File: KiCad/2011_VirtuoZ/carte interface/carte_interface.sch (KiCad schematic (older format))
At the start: 56 parts, among them P10 Convertisseur_I, P11 Convertisseur_U, P12 Convertisseur_PWM, P9 Vitesse, U3 LM358, U4 LM358

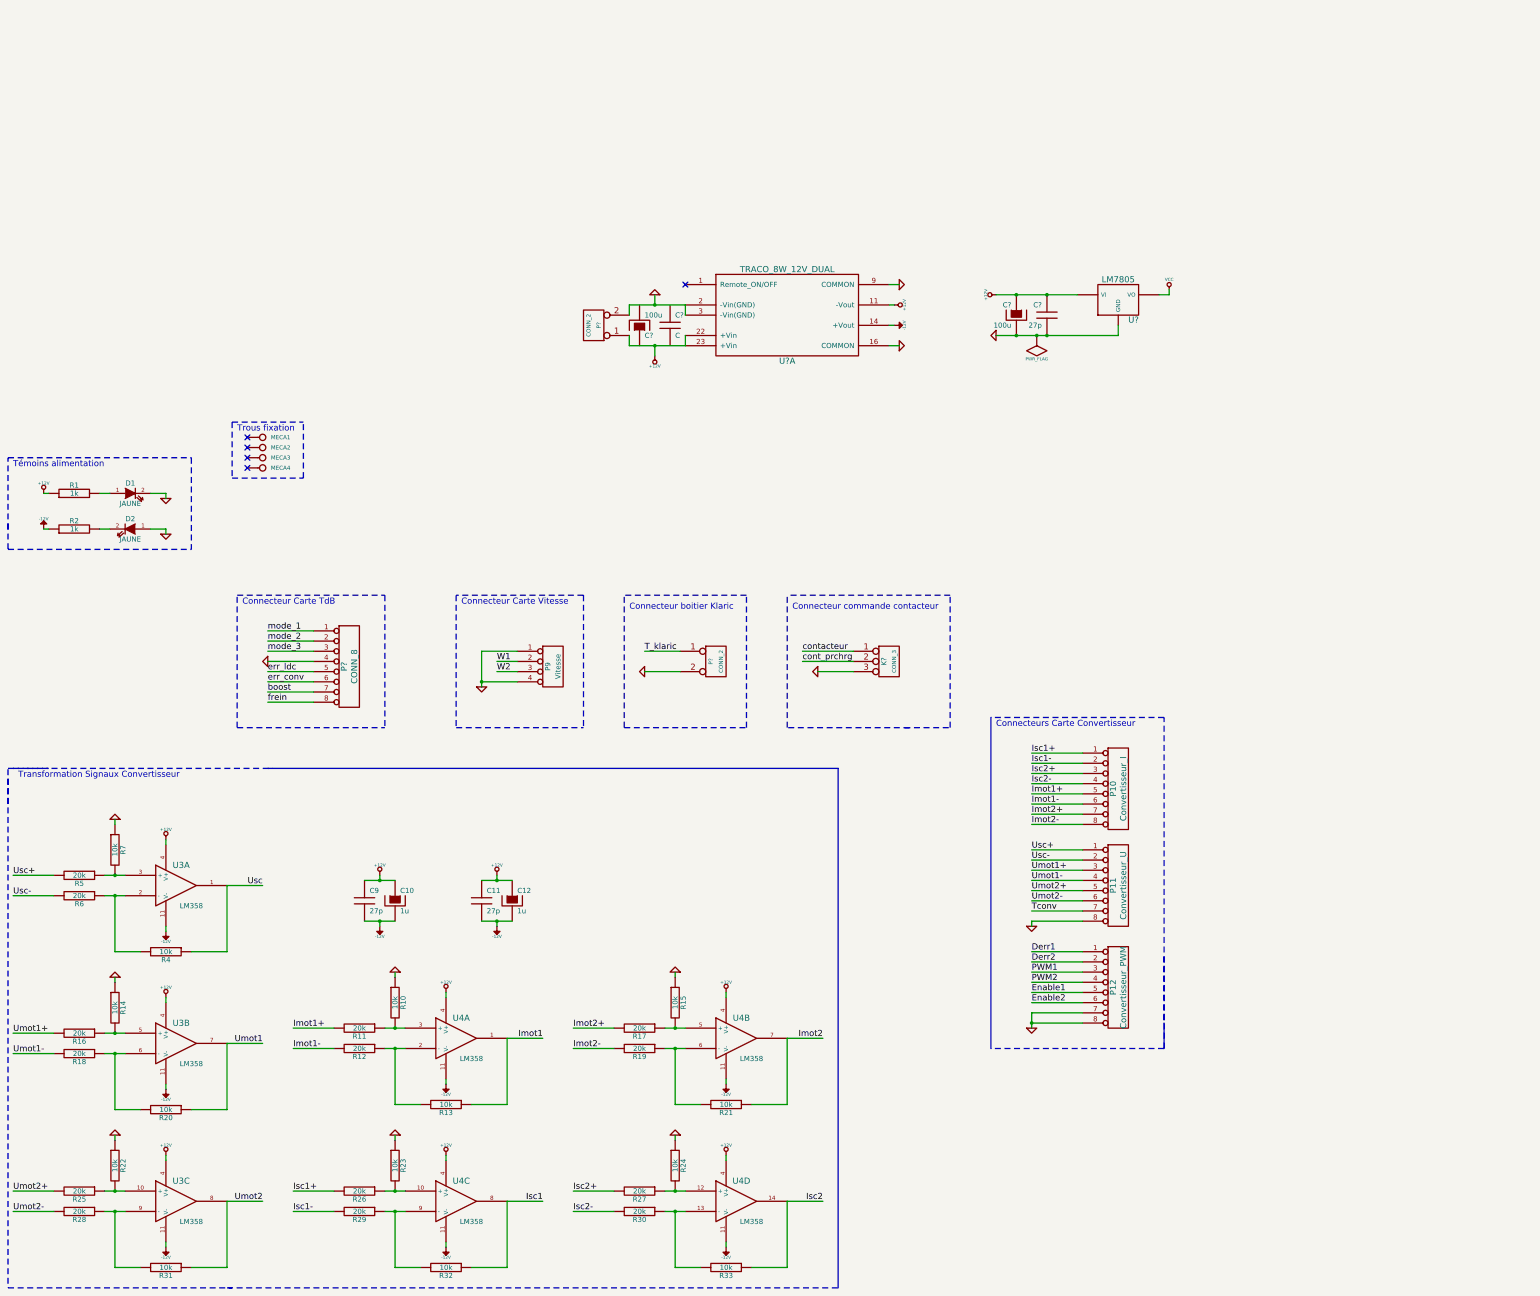
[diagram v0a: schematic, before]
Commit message: carte interface pliée
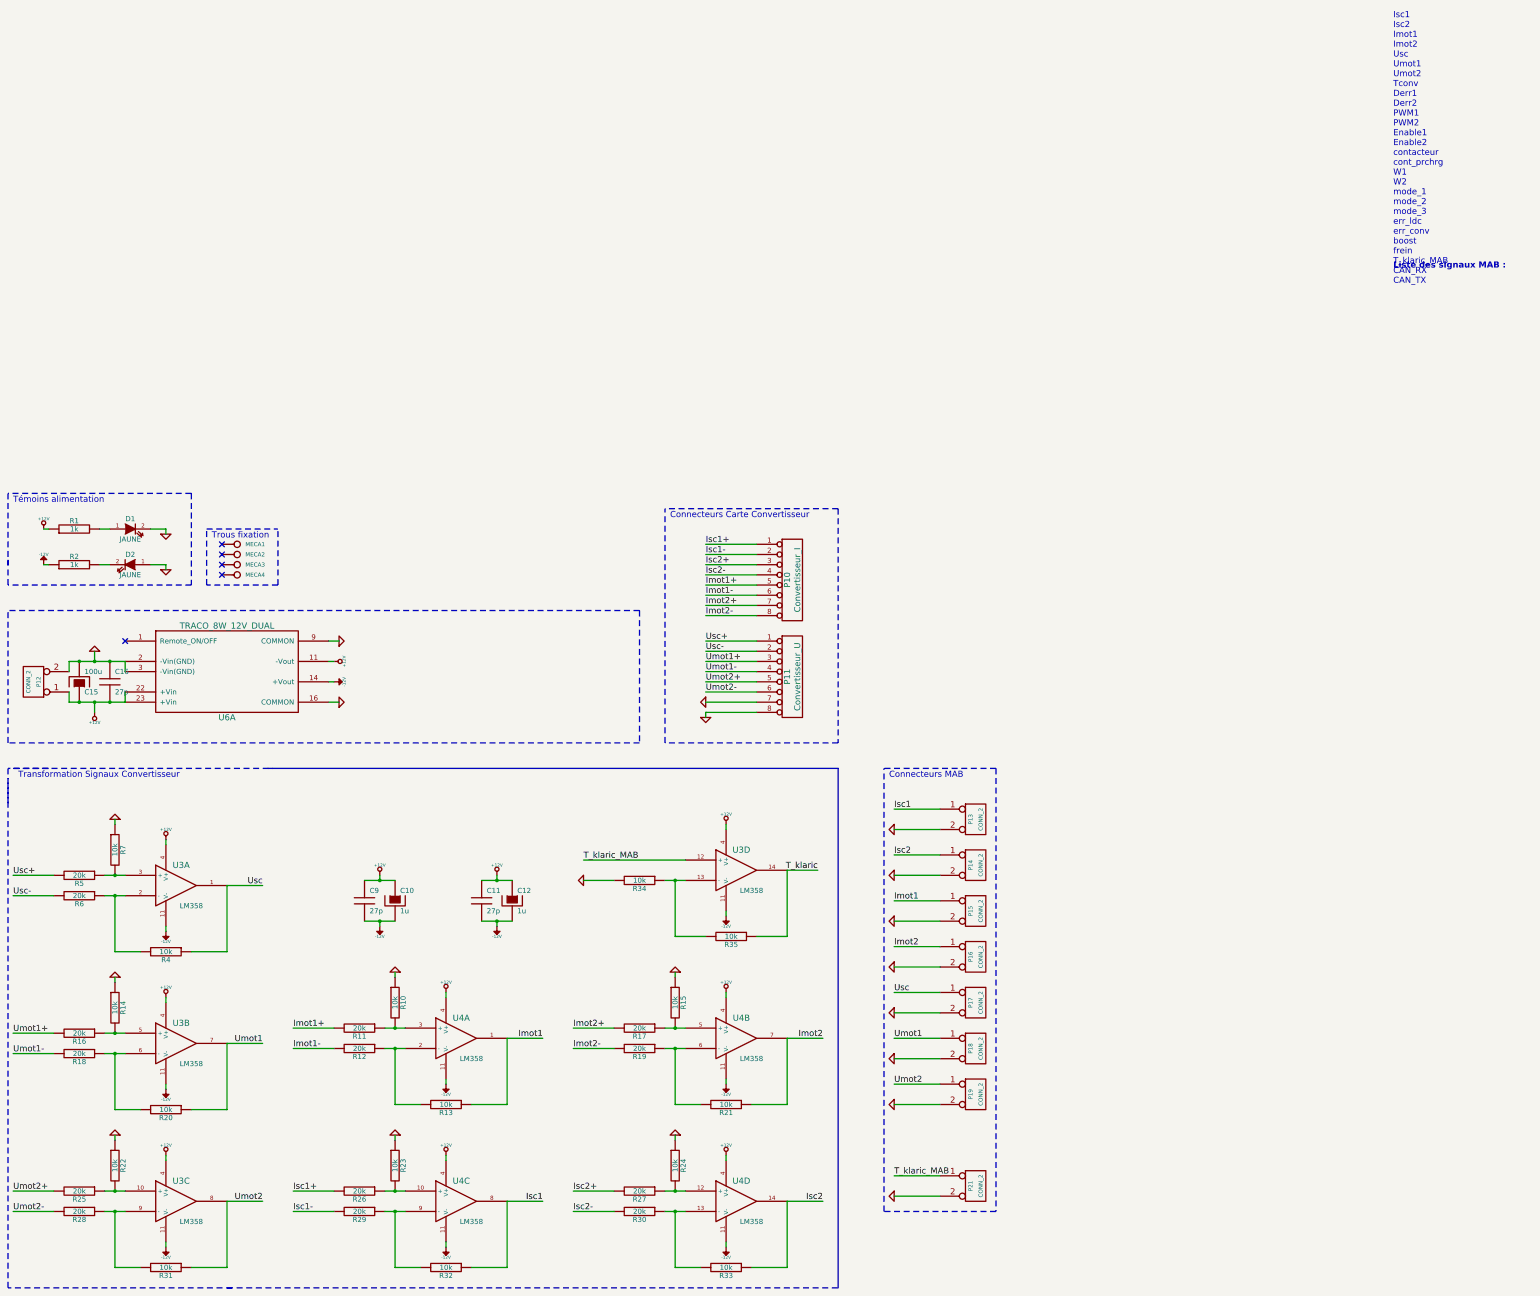
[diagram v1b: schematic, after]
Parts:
- removed C?: 100u, symbol CP
- removed C?: 27p, symbol C
- removed K?: CONN_3, symbol CONN_3
- removed P12: Convertisseur_PWM, symbol CONN_8
- removed P9: Vitesse, symbol CONN_4
- removed P?: CONN_8, symbol CONN_8
- removed U?: LM7805, symbol 7805
- added P13, P14, P15, P16, P17, P18, P19: CONN_2, symbol CONN_2
- added R34, R35: 10k, symbol R
- added unit 4 of U3
- C16: renamed from C?; value C -> 27p
- gave numbers to parts that had none: 4
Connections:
- net Tconv is gone; now on net GND: P11.7 (P7)
- net +12V: now also C15.1, C16.2, U3.4 (V+)
- net -12V: now also U3.11 (V-)
- net GND: now also C15.2, C16.1, P13.2 (PM), P14.2 (PM), P15.2 (PM), P16.2 (PM), P17.2 (PM), P18.2 (PM), P19.2 (PM), R34.2
- net Imot1: now also P15.1 (P1)
- net Imot2: now also P16.1 (P1)
- net Isc1: now also P13.1 (P1)
- net Isc2: now also P14.1 (P1)
- net T_klaric: now also R35.1, U3.14; no longer P21.1 (P1)
- net Umot1: now also P18.1 (P1)
- net Umot2: now also P19.1 (P1)
- net Usc: now also P17.1 (P1)
- new net: R34.1, R35.2, U3.13 (-)
- new net T_klaric_MAB: P21.1 (P1), U3.12 (+)
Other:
- note added: "Connecteurs MAB"
- note added: "Isc1\nIsc2\nImot1\nImot2\nUsc\nUmot1\nUmot2\nTconv\nDerr1\nDerr2\nPWM1\nPWM2\nEnable1\nEnable2\ncontacteur\ncont_prchrg\nW1\nW2\nmode_1\nmode_2\nmode_3\nerr_ldc\nerr_conv\nboost\nfrein\nT_klaric_MAB\nCAN_RX\nCAN_TX"
- note added: "Liste des signaux MAB :"
- note removed: "Connecteur Carte TdB"
- note removed: "Connecteur Carte Vitesse\n"
- note removed: "Connecteur boitier Klaric"
- note removed: "Connecteur commande contacteur"
- moved on the sheet: C15, C16, D1, D2, MECA1, MECA2, MECA3, MECA4, P10, P11, P12, P21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

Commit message: 
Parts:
- added P22: Alim MAB, symbol CONN_8
- added P23: Masse MAB, symbol CONN_8
- P12: value CONN_2 -> ALIM
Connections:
- net labels added: +12C
- wire segments 155 -> 173

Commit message: 
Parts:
- removed C10: 1u, symbol CP
- removed C9: 27p, symbol C
- removed P10: Convertisseur_I, symbol CONN_8
- removed P11: Convertisseur_U, symbol CONN_8
- removed P13, P14, P15, P16, P17, P18, P19, P21: CONN_2, symbol CONN_2
- removed R10, R13, R15, R21, R24, R33, R34, R35: 10k, symbol R
- removed R11, R12, R17, R19, R27, R30: 20k, symbol R
- removed unit 4 of U3
- removed unit 2 of U4
- removed unit 1 of U4
- removed unit 4 of U4
- added C? (x5): 330n, symbol C
- added C? (x5): 27p, symbol C
- added C? (x4): 1u, symbol CP
- added D? (x6): 1N4148, symbol DIODE
- added D?: ROUGE, symbol LED
- added K?: U_OUT, symbol CONN_3
- added MECA? (x2): MECA, symbol CONN_1
- added P?: Isc_IN, symbol CONN_2
- added P? (x3): Isc_OUT, symbol CONN_2
- added P? (x2): Imot1_IN, symbol CONN_2
- added P?: Tconv_IN, symbol CONN_2
- added P?: Umot1_IN, symbol CONN_2
- added P?: Umot2_IN, symbol CONN_2
- added P?: Tconv_OUT, symbol CONN_2
- added P?: CAN_1, symbol CONN_2
- added P?: CAN_2, symbol CONN_2
- added P?: CAN_MAB, symbol CONN_2
- added P?: Vitesse_IN, symbol CONN_4
- added P?: Vit_OUT, symbol CONN_2
- added P?: cont_IN, symbol CONN_2
- added P?: Cont_OUT, symbol CONN_4
- added P?: Drivers_IN, symbol CONN_8
- added P?: Drivers_OUT, symbol CONN_8
- added R? (x14): 1K, symbol R
- added R? (x6): 100, symbol R
- added R? (x12): 10K, symbol R
- added R? (x3): 5K, symbol R
- added R? (x4): 5k, symbol R
- added R? (x4): 20k, symbol R
- added R?: 1k, symbol R
- added U? (x14): LM358, symbol LM324
- added U?: 7805, symbol 7805
- C?: renamed from C16; value 27p -> 330n
- R?: renamed from R7; value 10k -> 5K
- R?: renamed from R4; value 10k -> 5K
- R?: renamed from R20; value 10k -> 5K
- R?: renamed from R14; value 10k -> 5K
- R?: renamed from R22; value 10k -> 5K
- R?: renamed from R31; value 10k -> 5K
- R?: renamed from R32; value 10k -> 5k
- R?: renamed from R23; value 10k -> 5k
- renumbered C12 to C?, C11 to C?, C15 to C?, D1 to D?, D2 to D?, MECA1 to MECA?, MECA2 to MECA?, MECA3 to MECA?, MECA4 to MECA?, P12 to P?, P22 to P?, P23 to P?, R1 to R?, R2 to R?, R5 to R?, R6 to R?, R18 to R?, R16 to R?, R25 to R?, R28 to R?, R29 to R?, R26 to R?, U3 to U?, U4 to U?, U6 to U?
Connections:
- net labels added: CONT+, ERR1, ERR2, INB1, INB2, Imot1_out, Imot1_sig, Imot2_out, Imot2_sig, Isc, Isc+, Isc-, Isc_out, Isc_sig, PRECH, PWM1, PWM2, VCC, W1, W2
- net labels removed: Isc1, Isc1+, Isc1-, Isc2, Isc2+, Isc2-, T_klaric, T_klaric_MAB
- wire segments 173 -> 436
- no-connect marks 5 -> 10
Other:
- note added: "Cartes drivers"
- note added: "Commande contacteurs"
- note added: "Désymétrisation"
- note added: "Filtrage 5KHz"
- note added: "Redressement"
- note added: "Splitter CAN"
- note added: "Traitement Imot1"
- note added: "Traitement Imot2"
- note added: "Traitement Isc"
- note added: "Traitement température"
- note added: "Traitement tensions"
- note added: "Transmission vitesse"
- note added: "o Isc\no Imot1\no Imot2\no Usc\no Umot1\no Umot2\no Tconv\no Derr1\no Derr2\no PWM1\no PWM2\no Enable1\no Enable2\no contacteur\no cont_prchrg\no W1\no W2\n- mode_1\n- mode_2\n- mode_3\n- err_MAB_1\n- err_MAB_2\n- err_MAB_3\n- boost\n- frein\no CAN_H\no CAN_L"
- note removed: "Connecteurs Carte Convertisseur"
- note removed: "Connecteurs MAB"
- note removed: "Isc1\nIsc2\nImot1\nImot2\nUsc\nUmot1\nUmot2\nTconv\nDerr1\nDerr2\nPWM1\nPWM2\nEnable1\nEnable2\ncontacteur\ncont_prchrg\nW1\nW2\nmode_1\nmode_2\nmode_3\nerr_ldc\nerr_conv\nboost\nfrein\nT_klaric_MAB\nCAN_RX\nCAN_TX"
- note removed: "Transformation Signaux Convertisseur"
- moved on the sheet: C?, D?, MECA?, P?, R?, U?A

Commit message: 
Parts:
- removed MECA? (x2): MECA, symbol CONN_1
- added P2: Err_OUT, symbol CONN_4
- added P26: Cont_OUT, symbol CONN_4
- added P28: Usc_IN, symbol CONN_2
- added P5: TDB_IN_OUT, symbol CONN_8
- added P7: Cmd_IN, symbol CONN_4
- P1: renamed from P?; value Cont_OUT -> Mode_IN
- P8: renamed from P?; value cont_IN -> Cont_IN
- gave numbers to parts that had none: 121
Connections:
- net labels added: boost, err_MAB1, err_MAB2, err_MAB3, frein, mode1, mode2, mode3
- wire segments 436 -> 373
- no-connect marks 10 -> 8
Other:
- note added: "Transmission TDB"
- note added: "o Isc\no Imot1\no Imot2\no Usc\no Umot1\no Umot2\no Tconv\no Derr1\no Derr2\no PWM1\no PWM2\no Enable1\no Enable2\no contacteur\no cont_prchrg\no W1\no W2\no mode_1\no mode_2\no mode_3\no err_MAB_1\no err_MAB_2\no err_MAB_3\no boost\no frein\no CAN_H\no CAN_L"
- note removed: "o Isc\no Imot1\no Imot2\no Usc\no Umot1\no Umot2\no Tconv\no Derr1\no Derr2\no PWM1\no PWM2\no Enable1\no Enable2\no contacteur\no cont_prchrg\no W1\no W2\n- mode_1\n- mode_2\n- mode_3\n- err_MAB_1\n- err_MAB_2\n- err_MAB_3\n- boost\n- frein\no CAN_H\no CAN_L"
- moved on the sheet: P1
